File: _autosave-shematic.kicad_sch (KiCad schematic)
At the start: 71 parts, among them J1 VIN, J10 FHOLD, J11 SRESU, J12 RESET, J13 Conn_02x03_Odd_Even, J14 Conn_02x03_Odd_Even, J15 Conn_02x03_Odd_Even, J16 X, J17 Y, J18 Z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

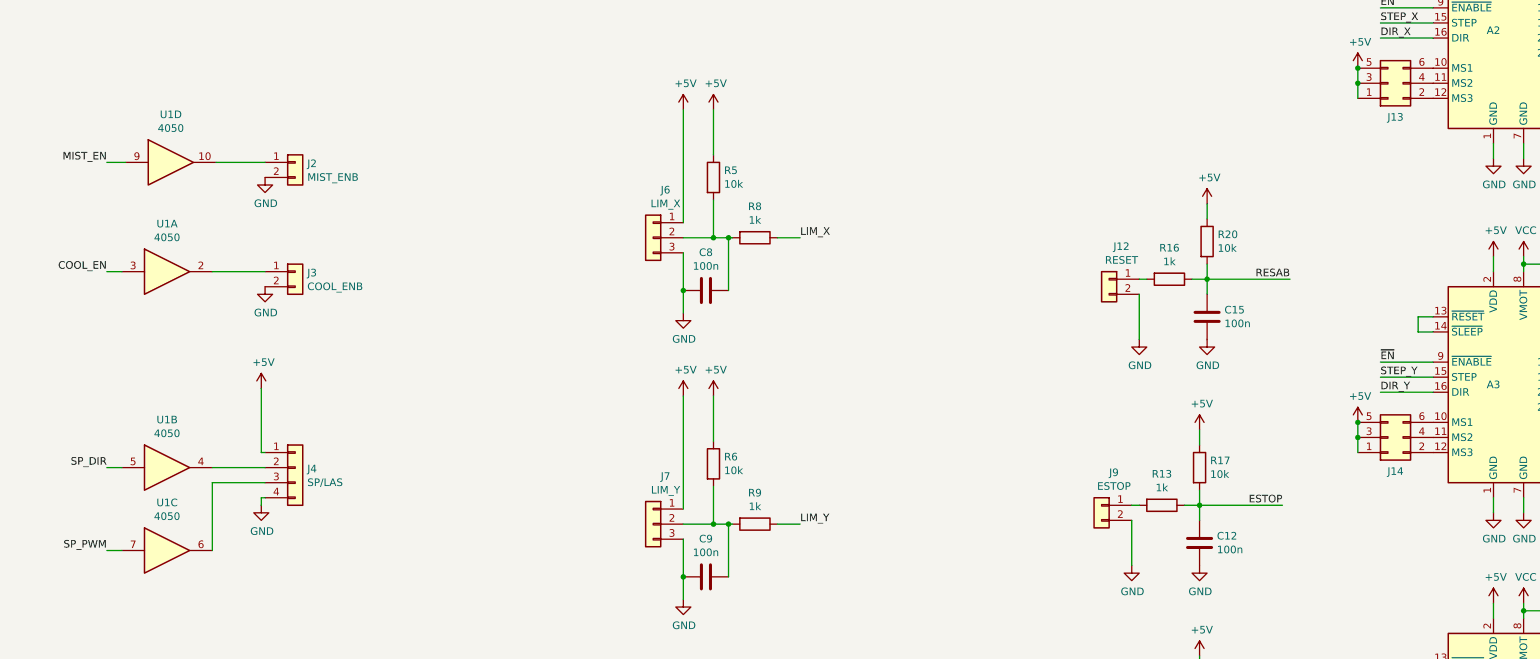
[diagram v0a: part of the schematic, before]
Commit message: replaced footprints for passive component, edited silkscreens
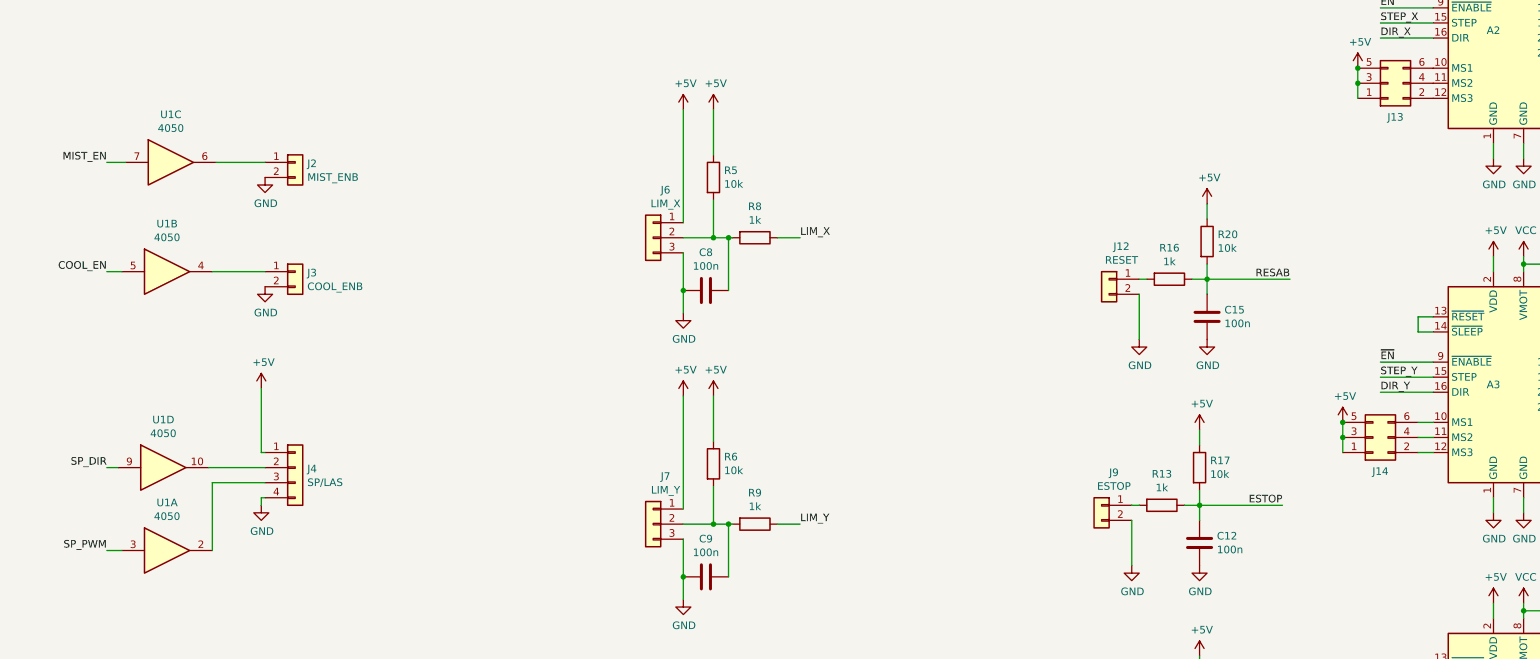
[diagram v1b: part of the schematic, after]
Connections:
- net COOL_EN: now also U1.5; no longer U1.3
- net MIST_EN: now also U1.7; no longer U1.9
- net SP_DIR: now also U1.9; no longer U1.5
- net SP_PWM: now also U1.3; no longer U1.7
- net at U1.2: now also J4.3 (Pin_3); no longer J3.1 (Pin_1)
- net at U1.4: now also J3.1 (Pin_1); no longer J4.2 (Pin_2)
- net at U1.6: now also J2.1 (Pin_1); no longer J4.3 (Pin_3)
- net at U1.10: now also J4.2 (Pin_2); no longer J2.1 (Pin_1)
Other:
- moved on the sheet: J14, U1A, U1B, U1C, U1D
